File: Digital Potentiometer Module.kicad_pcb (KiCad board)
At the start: 2 copper layers, 0 parts

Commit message: design pcb
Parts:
- added C1: 10uF, Capacitor_SMD:CP_Elec_5x5.3, F.Cu at (120.9, 85.6)
- added C2: 10uF, Capacitor_SMD:CP_Elec_5x5.3, F.Cu at (120.9, 94.7)
- added D1: LED, LED_SMD:LED_0603_1608Metric_Pad1.05x0.95mm_HandSolder, F.Cu at (120.2, 105.3)
- added D2: D, Custom:SK55-DO214AA, F.Cu at (132.8, 129.5)
- added J1: Barrel_Jack (>5V), Connector_BarrelJack:BarrelJack_CLIFF_FC681465S_SMT_Horizontal, F.Cu at (143.5, 129.0)
- added J2: Conn_01x04_Pin, Connector_PinHeader_2.54mm:PinHeader_1x04_P2.54mm_Vertical, F.Cu at (118.7, 134.1)
- added J3: Conn_01x02_Pin, Connector_PinHeader_2.54mm:PinHeader_1x02_P2.54mm_Vertical, F.Cu at (163.2, 134.1)
- added J4: Conn_01x03_Pin, Connector_PinHeader_2.54mm:PinHeader_1x03_P2.54mm_Vertical, F.Cu at (155.1, 134.1)
- added R1: 10K, Resistor_SMD:R_0805_2012Metric_Pad1.20x1.40mm_HandSolder, F.Cu at (156.7, 120.7)
- added R2: 360, Resistor_SMD:R_0805_2012Metric_Pad1.20x1.40mm_HandSolder, F.Cu at (120.2, 111.4)
- added R3: 10K, Resistor_SMD:R_0805_2012Metric_Pad1.20x1.40mm_HandSolder, F.Cu at (161.7, 120.7)
- added R4: 220, Resistor_SMD:R_0805_2012Metric_Pad1.20x1.40mm_HandSolder, F.Cu at (135.4, 106.9)
- added R5: 360, Resistor_SMD:R_0805_2012Metric_Pad1.20x1.40mm_HandSolder, F.Cu at (135.4, 112.0)
- added S1: Slide Switch, Custom:Switch_Slide_8.5x3.5mm, F.Cu at (126.1, 130.9)
- added SW1: SW_SPST, Button_Switch_SMD:SW_SPST_PTS645, F.Cu at (159.3, 111.3)
- added SW2: SW_SPST, Button_Switch_SMD:SW_SPST_PTS645, F.Cu at (159.3, 96.0)
- added U1: ESP32-WROOM-32E, RF_Module:ESP32-WROOM-32D, F.Cu at (141.0, 90.8)
- added U2: AD5231BRUZ10, AD5231BRUZ10:SOP65P640X120-16N, F.Cu at (159.3, 84.6)
- added U3: LM317_SOT-223, Package_TO_SOT_SMD:SOT-223-3_TabPin2, F.Cu at (143.8, 109.6)
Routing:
- net /3.3V: track 0.00 -> 162.6 mm, vias 0 -> 5
- net GND: track 0.00 -> 84.4 mm, vias 0 -> 8
- net /EN: track 0.00 -> 70.1 mm, vias 0 -> 3
- net /POT_WIPER: track 0.00 -> 68.0 mm, vias 0 -> 4
- net /TX: track 0.00 -> 62.9 mm, vias 0 -> 2
- net /ENC_A: track 0.00 -> 60.2 mm, vias 0 -> 2
- net /POT_A: track 0.00 -> 60.1 mm, vias 0 -> 2
- net /RX: track 0.00 -> 58.8 mm, vias 0 -> 2
- net /ENC_B: track 0.00 -> 56.8 mm, vias 0 -> 2
- net /POT_B: track 0.00 -> 56.3 mm
- net /CTS: track 0.00 -> 46.5 mm, vias 0 -> 2
- net /BOOT: track 0.00 -> 38.0 mm
- net /RTS: track 0.00 -> 34.8 mm, vias 0 -> 2
- net /VIN: track 0.00 -> 28.0 mm
- net /SCLK: track 0.00 -> 15.1 mm, vias 0 -> 2
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- added copper zone on B.Cu, net GND
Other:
- board outline added: 49.5 x 78.2 mm
- board text added: "3.3V"
- board text added: ">3.3V"
- board text added: "A"
- board text added: "B"
- board text added: "BOOT"
- board text added: "CTS"
- board text added: "EN"
- board text added: "ENC"
- board text added: "POT"
- board text added: "RTS"
- board text added: "RX"
- board text added: "TX"
- board text added: "W"

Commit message: make improvements to pcb
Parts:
- removed J3: Conn_01x02_Pin, Connector_PinHeader_2.54mm:PinHeader_1x02_P2.54mm_Vertical
- added J5: Conn_01x03_Pin, Connector_PinHeader_2.54mm:PinHeader_1x03_P2.54mm_Vertical, F.Cu at (163.3, 129.2)
- S1: footprint Custom:Switch_Slide_8.5x3.5mm -> digikey-footprints:Switch_Slide_11.6x4mm_EG1218
- U1: footprint RF_Module:ESP32-WROOM-32D -> Custom:XCVR_ESP32-WROOM-32E__4MB_
- moved S1 2.72 mm to (126.2, 128.2)
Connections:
- net /J_POS renamed /PD_IN
- net Net-(D2-K) renamed /PD_OUT
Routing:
- net /3.3V: track 162.6 -> 152.2 mm, vias 5 -> 4
- net /ENC_A: track 60.2 -> 53.2 mm, vias 2 -> 1
- net /RX: track 58.8 -> 52.7 mm
- net /PD_IN: track 5.59 -> 11.6 mm
- net /TX: track 62.9 -> 57.4 mm
- net /EN: track 70.1 -> 65.0 mm, vias 3 -> 4
- net /BOOT: track 38.0 -> 34.0 mm
- net /CS: track 13.2 -> 15.4 mm, vias 0 -> 2
- net /CTS: track 46.5 -> 45.3 mm
- net /SCLK: track 15.1 -> 16.3 mm, vias 2 -> 0
- net /MOSI: track 14.7 -> 16.0 mm
- net /RTS: track 34.8 -> 33.6 mm
- net /PD_OUT: track 6.88 -> 7.92 mm
- net GND: track 84.4 -> 83.9 mm
- net /ENC_B: track 56.8 -> 56.5 mm, vias 2 -> 1
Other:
- board size 49.5 x 78.2 mm -> 49.5 x 59.8 mm
- board text added: "GND"
- board text added: "TODO: 1. Choose bigger components when too small 2. Measure footprints with real components 3. Check wiring"

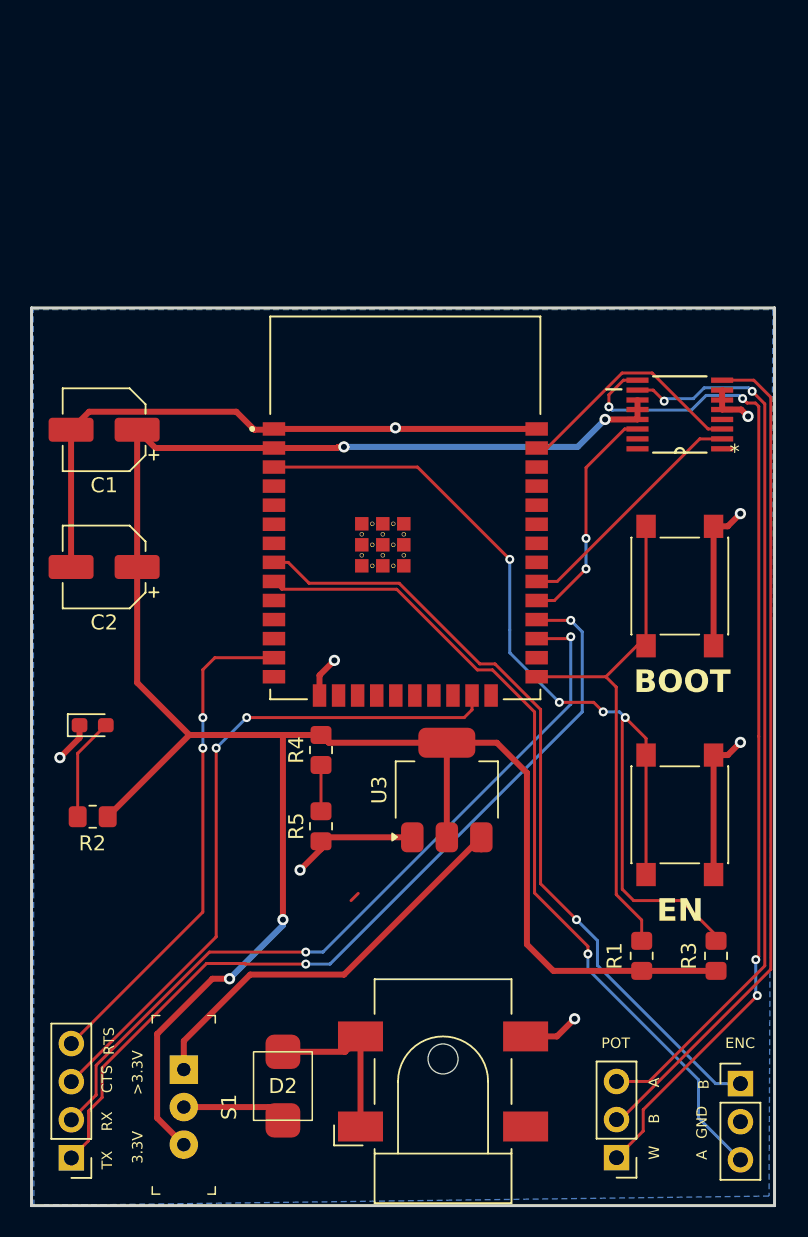
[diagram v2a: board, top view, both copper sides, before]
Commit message: fix design issues
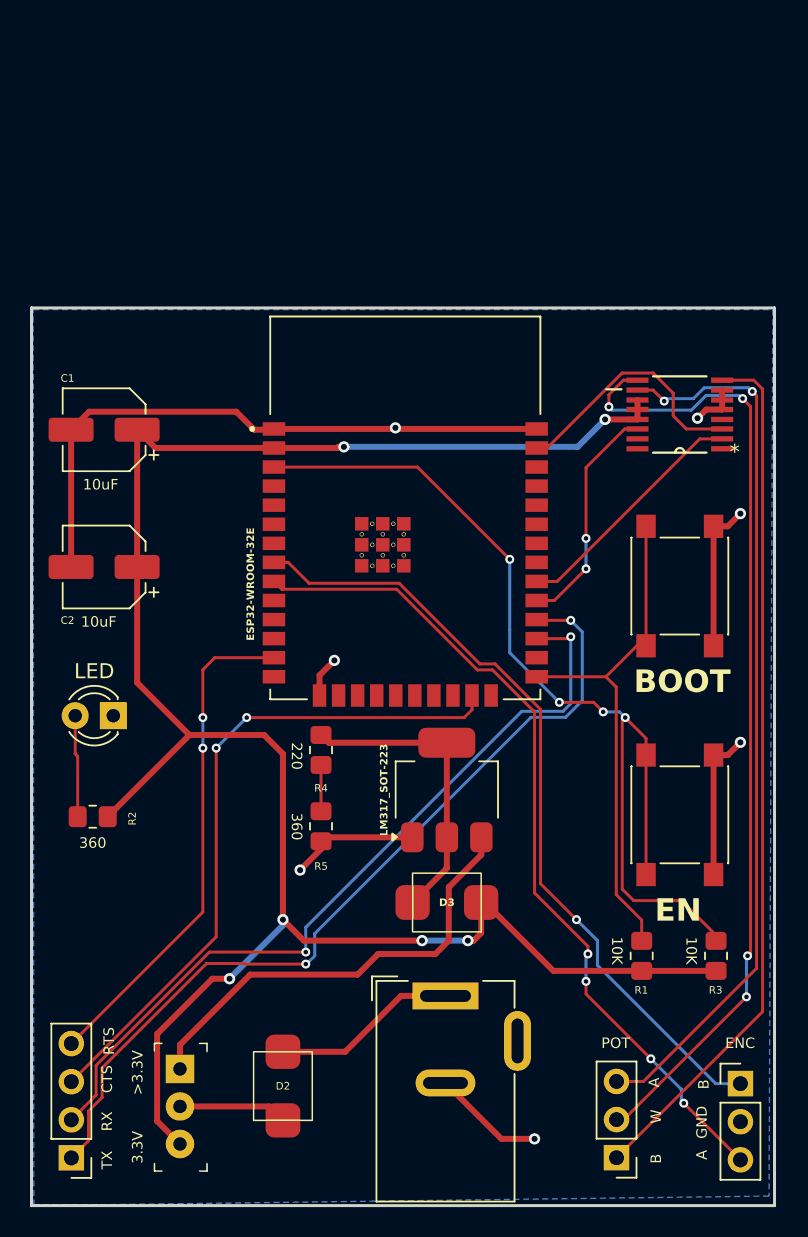
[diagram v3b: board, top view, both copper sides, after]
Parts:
- added D3: 40V 2A, Custom:SK55-DO214AA, F.Cu at (144.0, 117.1)
- D1: footprint LED_SMD:LED_0603_1608Metric_Pad1.05x0.95mm_HandSolder -> LED_THT:LED_D3.0mm
- D2: value D -> 40V 2A
- J1: footprint Connector_BarrelJack:BarrelJack_CLIFF_FC681465S_SMT_Horizontal -> Connector_BarrelJack:BarrelJack_Wuerth_6941xx301002
- S1: footprint digikey-footprints:Switch_Slide_11.6x4mm_EG1218 -> Custom:Switch_Slide_8.5x3.5mm
- moved J1 5.70 mm to (143.7, 123.3), turned to 0 degrees
- moved S1 2.49 mm to (125.9, 130.7)
- moved D1 1.52 mm to (121.5, 104.6), turned to 180 degrees
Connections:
- J1 pad 3: (no net) -> unconnected-(J1-Pad3)
- J4 pad 1: /POT_WIPER -> /POT_B
- J4 pad 2: /POT_B -> /POT_WIPER
- R4 pad 1: /3.3V -> /REG_OUT
- U3 pad 2: /3.3V -> /REG_OUT
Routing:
- net /REG_OUT: track 0.00 -> 20.2 mm
- net /3.3V: track 152.2 -> 136.5 mm, vias 4 -> 6
- net /POT_WIPER: track 68.0 -> 65.0 mm
- net /VIN: track 28.2 -> 31.0 mm
- net /POT_B: track 56.3 -> 58.2 mm
- net /RX: track 52.7 -> 53.7 mm
- net /MOSI: track 16.0 -> 16.9 mm
- net /PD_IN: track 11.6 -> 12.4 mm
- net (no net): track 0.68 -> 0.00 mm
- net /POT_A: track 60.1 -> 59.4 mm
- net GND: track 83.9 -> 83.5 mm, vias 8 -> 7
- net /ENC_B: track 56.5 -> 56.6 mm, vias 1 -> 4
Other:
- board text added: "10K"
- board text added: "10uF"
- board text added: "220"
- board text added: "360"
- board text removed: "TODO: 1. Choose bigger components when too small 2. Measure footprints with real components 3. Check wiring"

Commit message: fix bugs with pcb design
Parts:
- R5: value 360 -> 470
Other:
- board text added: "470"
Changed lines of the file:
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@@
 			)
 		)
-		(property "Value" "360"
+		(property "Value" "470"
 			(at 0 1.65 90)
 			(layer "F.Fab")
@@
 		)
 	)
-	(gr_text "360"
+	(gr_text "470"
 		(at 133.35 111.125 270)
 		(layer "F.SilkS")

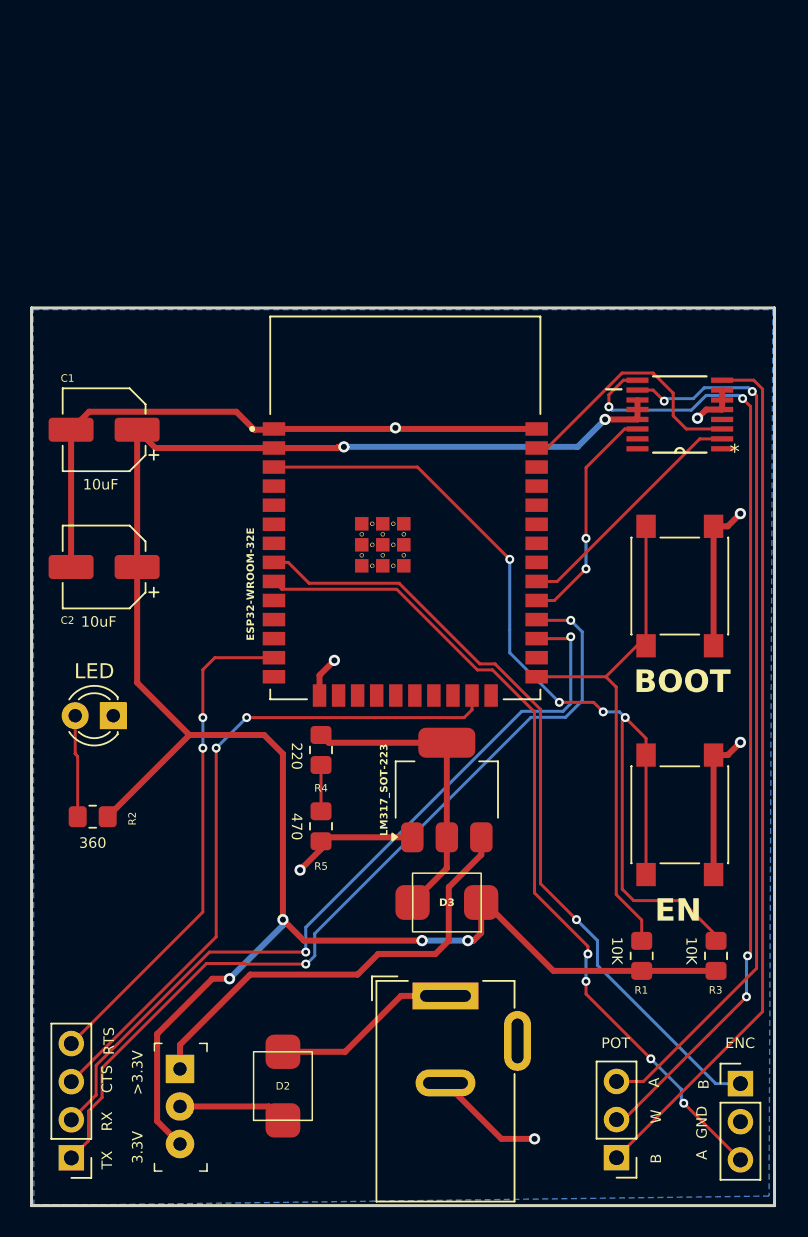
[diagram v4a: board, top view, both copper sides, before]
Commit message: fix UART communication pins
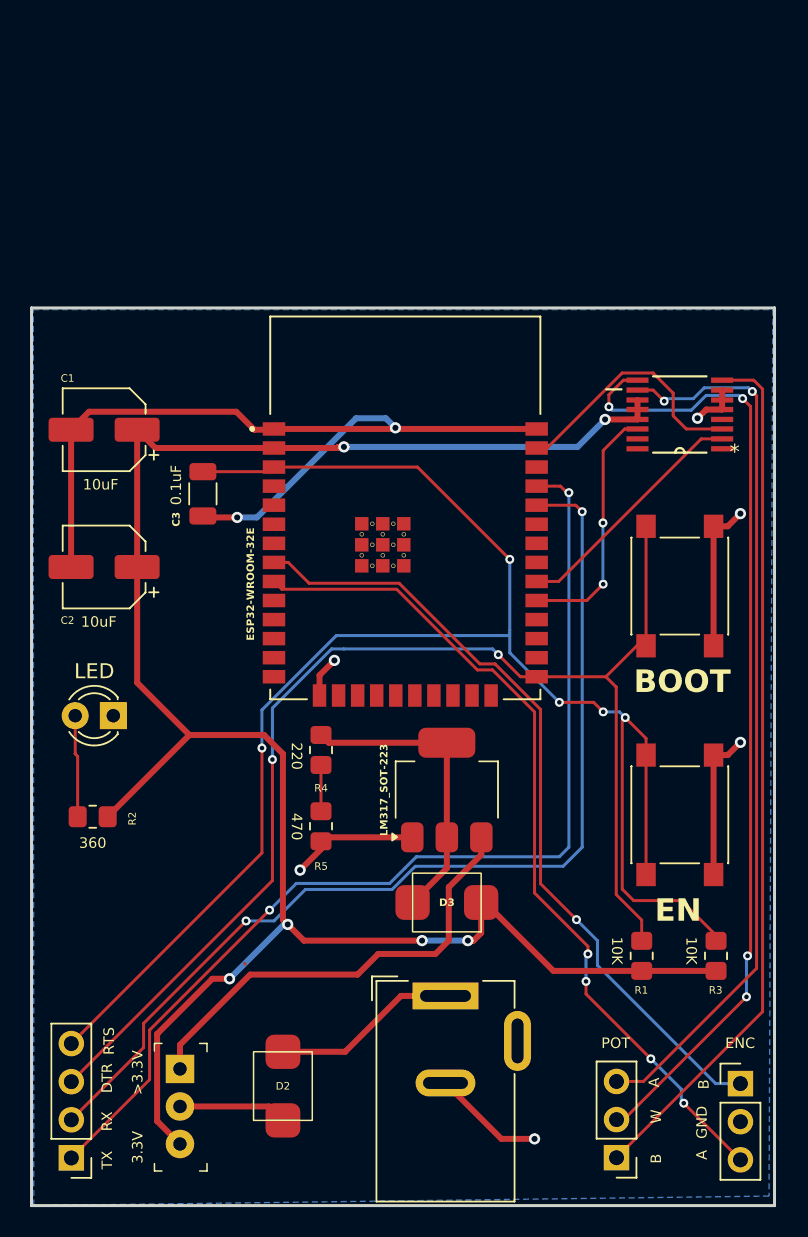
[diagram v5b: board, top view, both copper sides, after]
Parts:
- added C3: 0.1uF, Capacitor_SMD:C_1206_3216Metric, F.Cu at (127.5, 89.9)
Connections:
- J2 pad 3: /CTS -> /BOOT
- J2 pad 4: /RTS -> /EN
- U1 pad 13: /RTS -> unconnected-(U1-IO14-Pad13)
- U1 pad 23: /CTS -> unconnected-(U1-IO15-Pad23)
- U1 pad 27: /RX -> unconnected-(U1-IO16-Pad27)
- U1 pad 28: /TX -> unconnected-(U1-IO17-Pad28)
- U1 pad 34: unconnected-(U1-RXD0/IO3-Pad34) -> /RX
- U1 pad 35: unconnected-(U1-TXD0/IO1-Pad35) -> /TX
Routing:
- net /EN: track 65.0 -> 115.9 mm, vias 4 -> 5
- net /BOOT: track 34.0 -> 84.5 mm, vias 0 -> 2
- net /CTS: track 45.3 -> 0.00 mm, vias 2 -> 0
- net /RTS: track 33.6 -> 0.00 mm, vias 2 -> 0
- net GND: track 83.5 -> 99.4 mm, vias 7 -> 8
- net /RX: track 53.7 -> 68.1 mm
- net /TX: track 57.8 -> 69.7 mm
- net /CS: track 15.4 -> 16.7 mm
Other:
- board text added: "DTR"
- board text removed: "CTS"

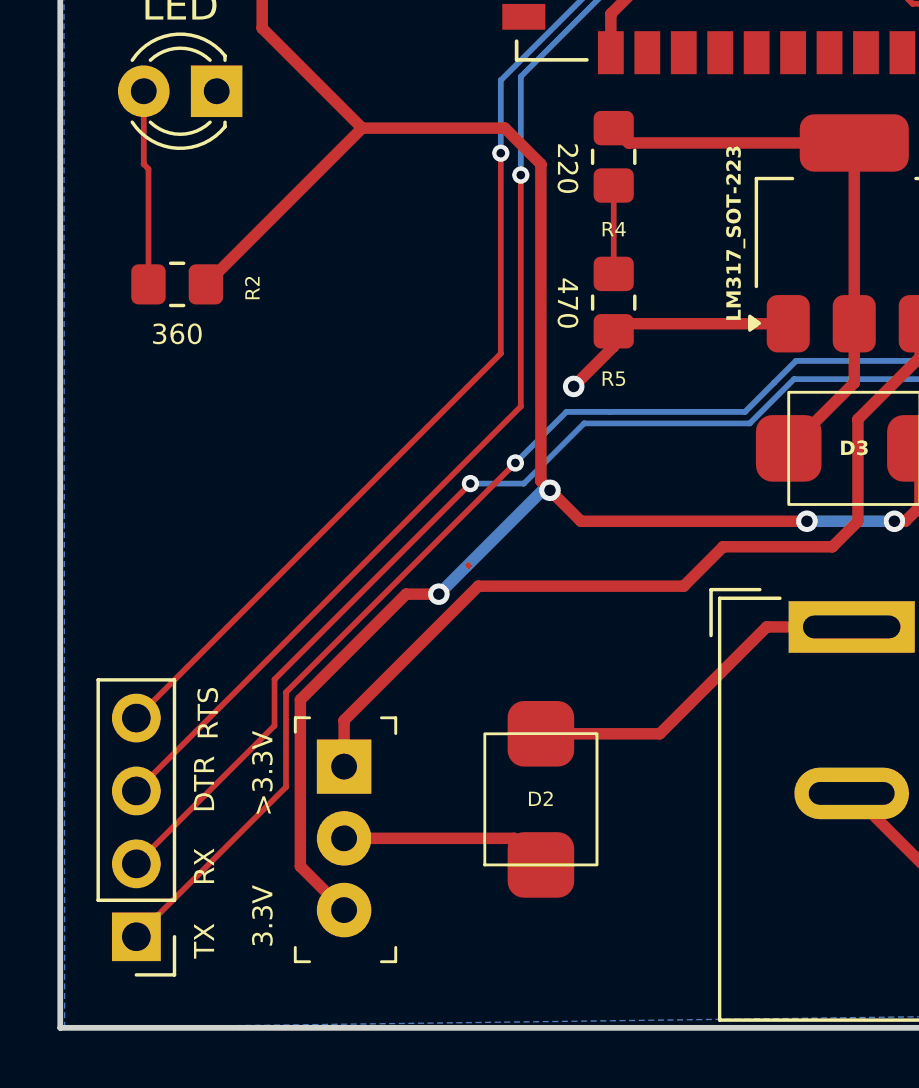
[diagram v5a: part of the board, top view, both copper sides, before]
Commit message: add vcc, gnd pins. change dtr pin to cts
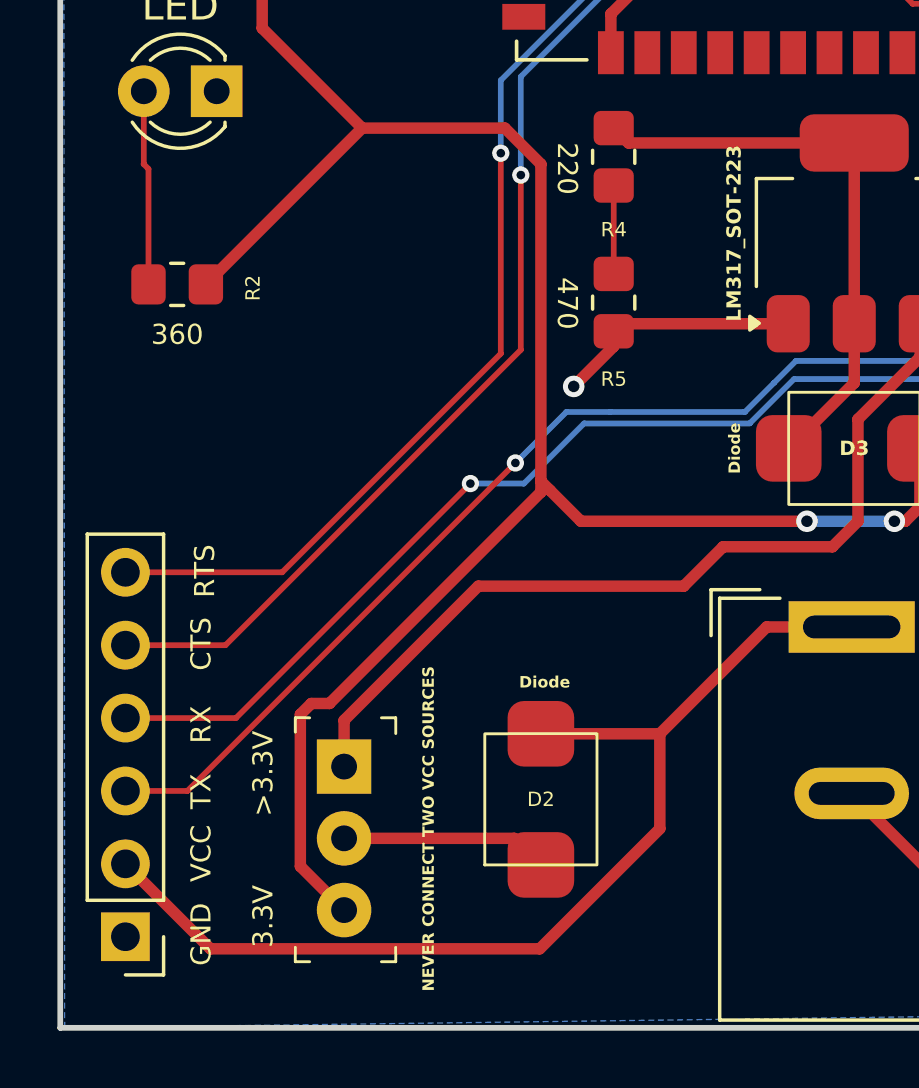
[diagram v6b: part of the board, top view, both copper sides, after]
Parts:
- J2: value Conn_01x04_Pin -> Conn_01x06_Pin; footprint Connector_PinHeader_2.54mm:PinHeader_1x04_P2.54mm_Vertical -> Connector_PinHeader_2.54mm:PinHeader_1x06_P2.54mm_Vertical
- moved J2 0.38 mm to (118.4, 134.1)
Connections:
- net /VIN renamed /VCC
- J2 pad 1: /TX -> GND
- J2 pad 2: /RX -> /PD_IN
- J2 pad 3: /BOOT -> /TX
- J2 pad 4: /EN -> /RX
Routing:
- net /PD_IN: track 12.4 -> 37.3 mm
- net /TX: track 69.7 -> 65.9 mm
- net /BOOT: track 84.5 -> 81.6 mm
- net /RX: track 68.1 -> 65.4 mm
- net /EN: track 115.9 -> 114.2 mm
- net /3.3V: track 136.4 -> 136.2 mm, vias 6 -> 4
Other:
- board text added: "CTS"
- board text added: "Digital Potentiometer Module"
- board text added: "Diode"
- board text added: "NEVER CONNECT TWO VCC SOURCES"
- board text added: "V1"
- board text added: "VCC"
- board text removed: "DTR"

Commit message: fix issues with serial communication pins
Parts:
- J1: value Barrel_Jack (>5V) -> Barrel_Jack
- S1: footprint Custom:Switch_Slide_8.5x3.5mm -> Connector_PinHeader_2.54mm:PinHeader_1x03_P2.54mm_Vertical
- moved S1 3.03 mm to (126.0, 127.7), turned to 0 degrees
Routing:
- net /VCC: track 31.0 -> 30.5 mm
- net /3.3V: track 136.2 -> 135.7 mm
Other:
- board text added: "390"
- board text added: "3mm"
- board text added: "5V"
- board text added: "DTR"
- board text added: "rev 0.1"
- board text removed: "360"
- board text removed: ">3.3V"
- board text removed: "CTS"
- board text removed: "V1"

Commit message: improve pcb design
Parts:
- added C4: 0.1uF, Capacitor_SMD:C_1206_3216Metric, F.Cu at (127.5, 95.3)
- C2: value 10uF -> 22uF
- R2: value 360 -> 390
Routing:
- net /3.3V: track 135.7 -> 140.9 mm
- net GND: track 99.4 -> 101.9 mm
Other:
- board text added: "22uF"
